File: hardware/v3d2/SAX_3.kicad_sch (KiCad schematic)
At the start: 92 parts, among them J1 joystick, J2 LED strip, J3 SSD1306 SPI, J4 MIDI OUT Y:M5 - R:M4, J5 Batt, J6 Neck - Y:O BK:B R:3.3, Q1 2N7000, U1 74HC165, U2 74HC165, U3 74HC165, U4 Teensy3.2_breadboard_friendly

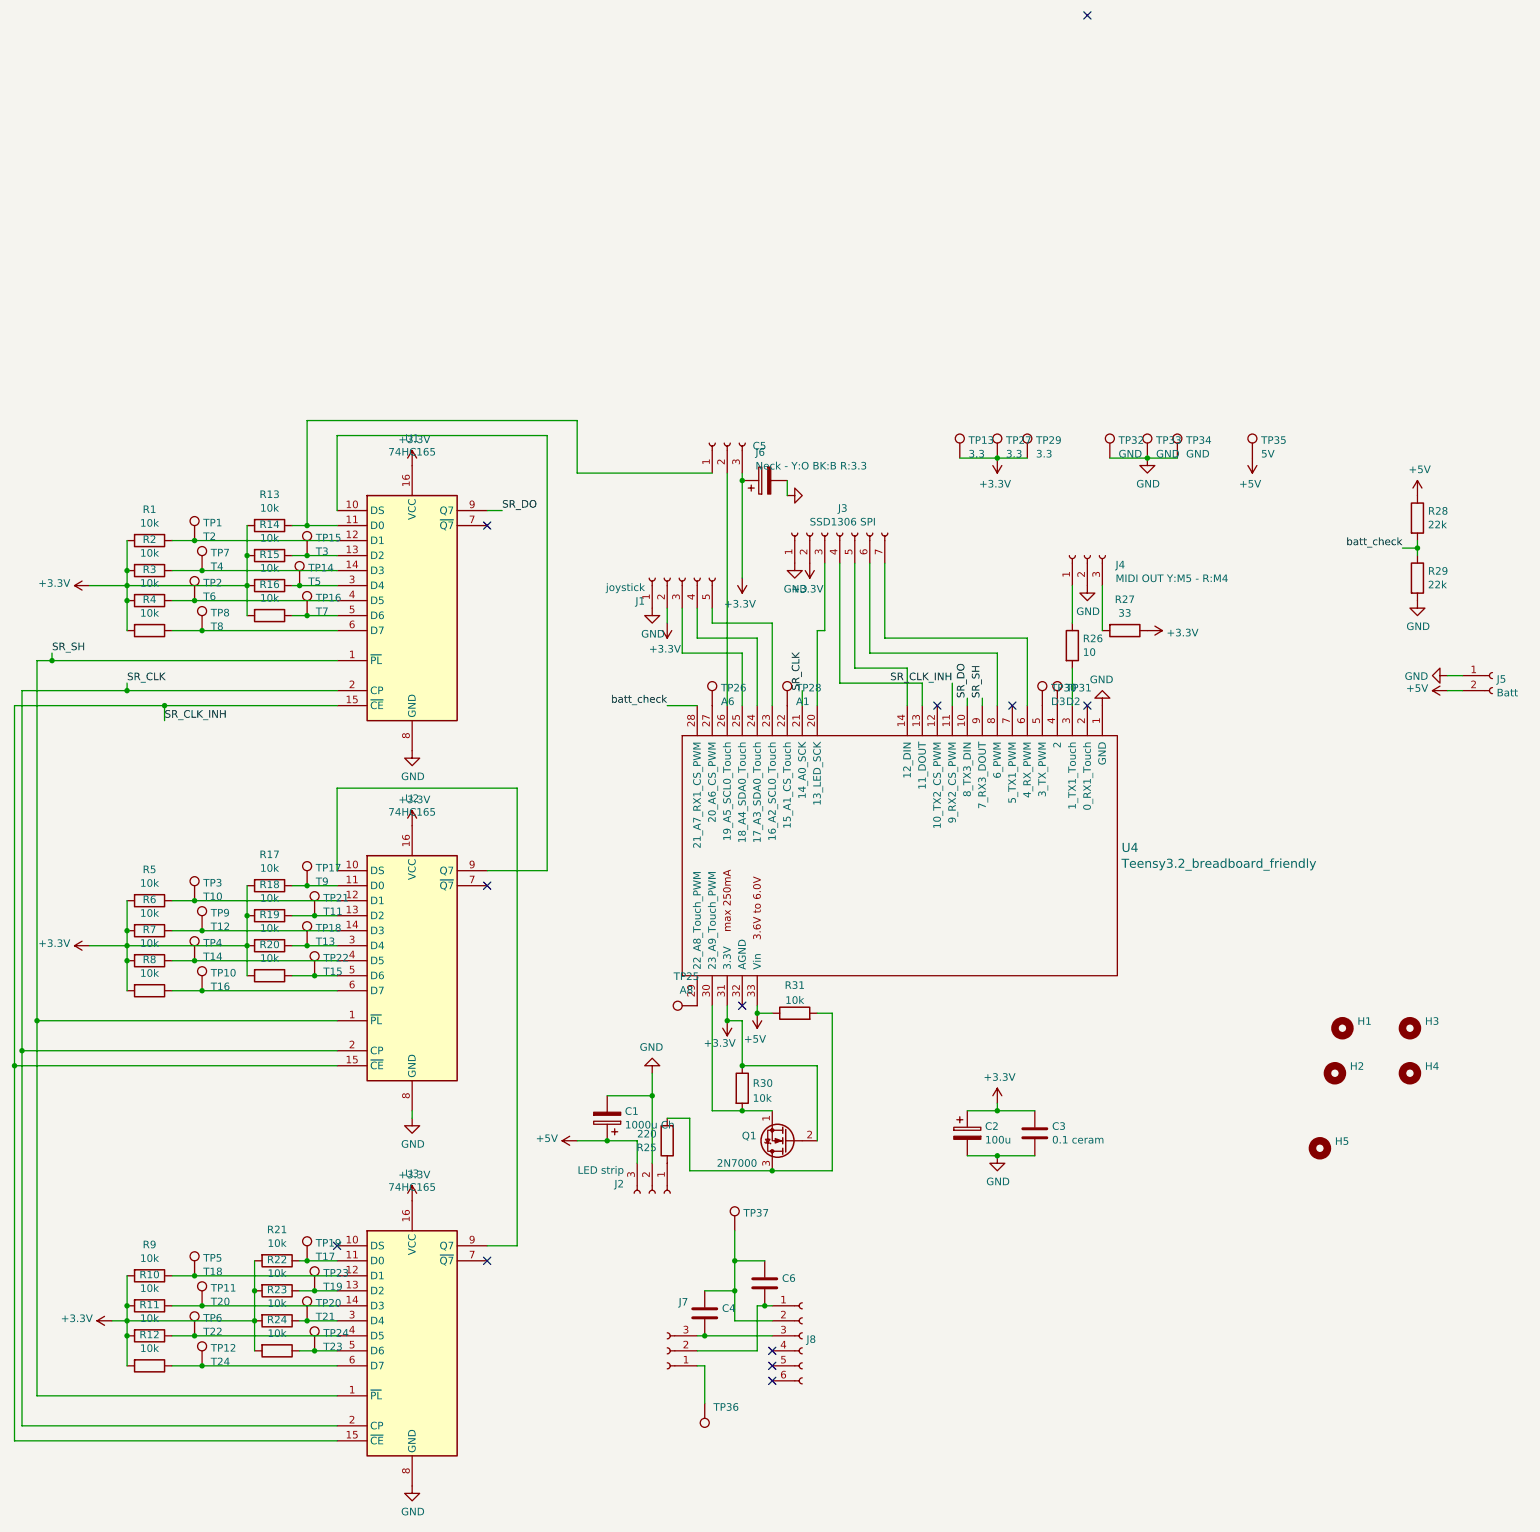
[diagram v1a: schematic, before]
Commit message: Added ADC component for battery check
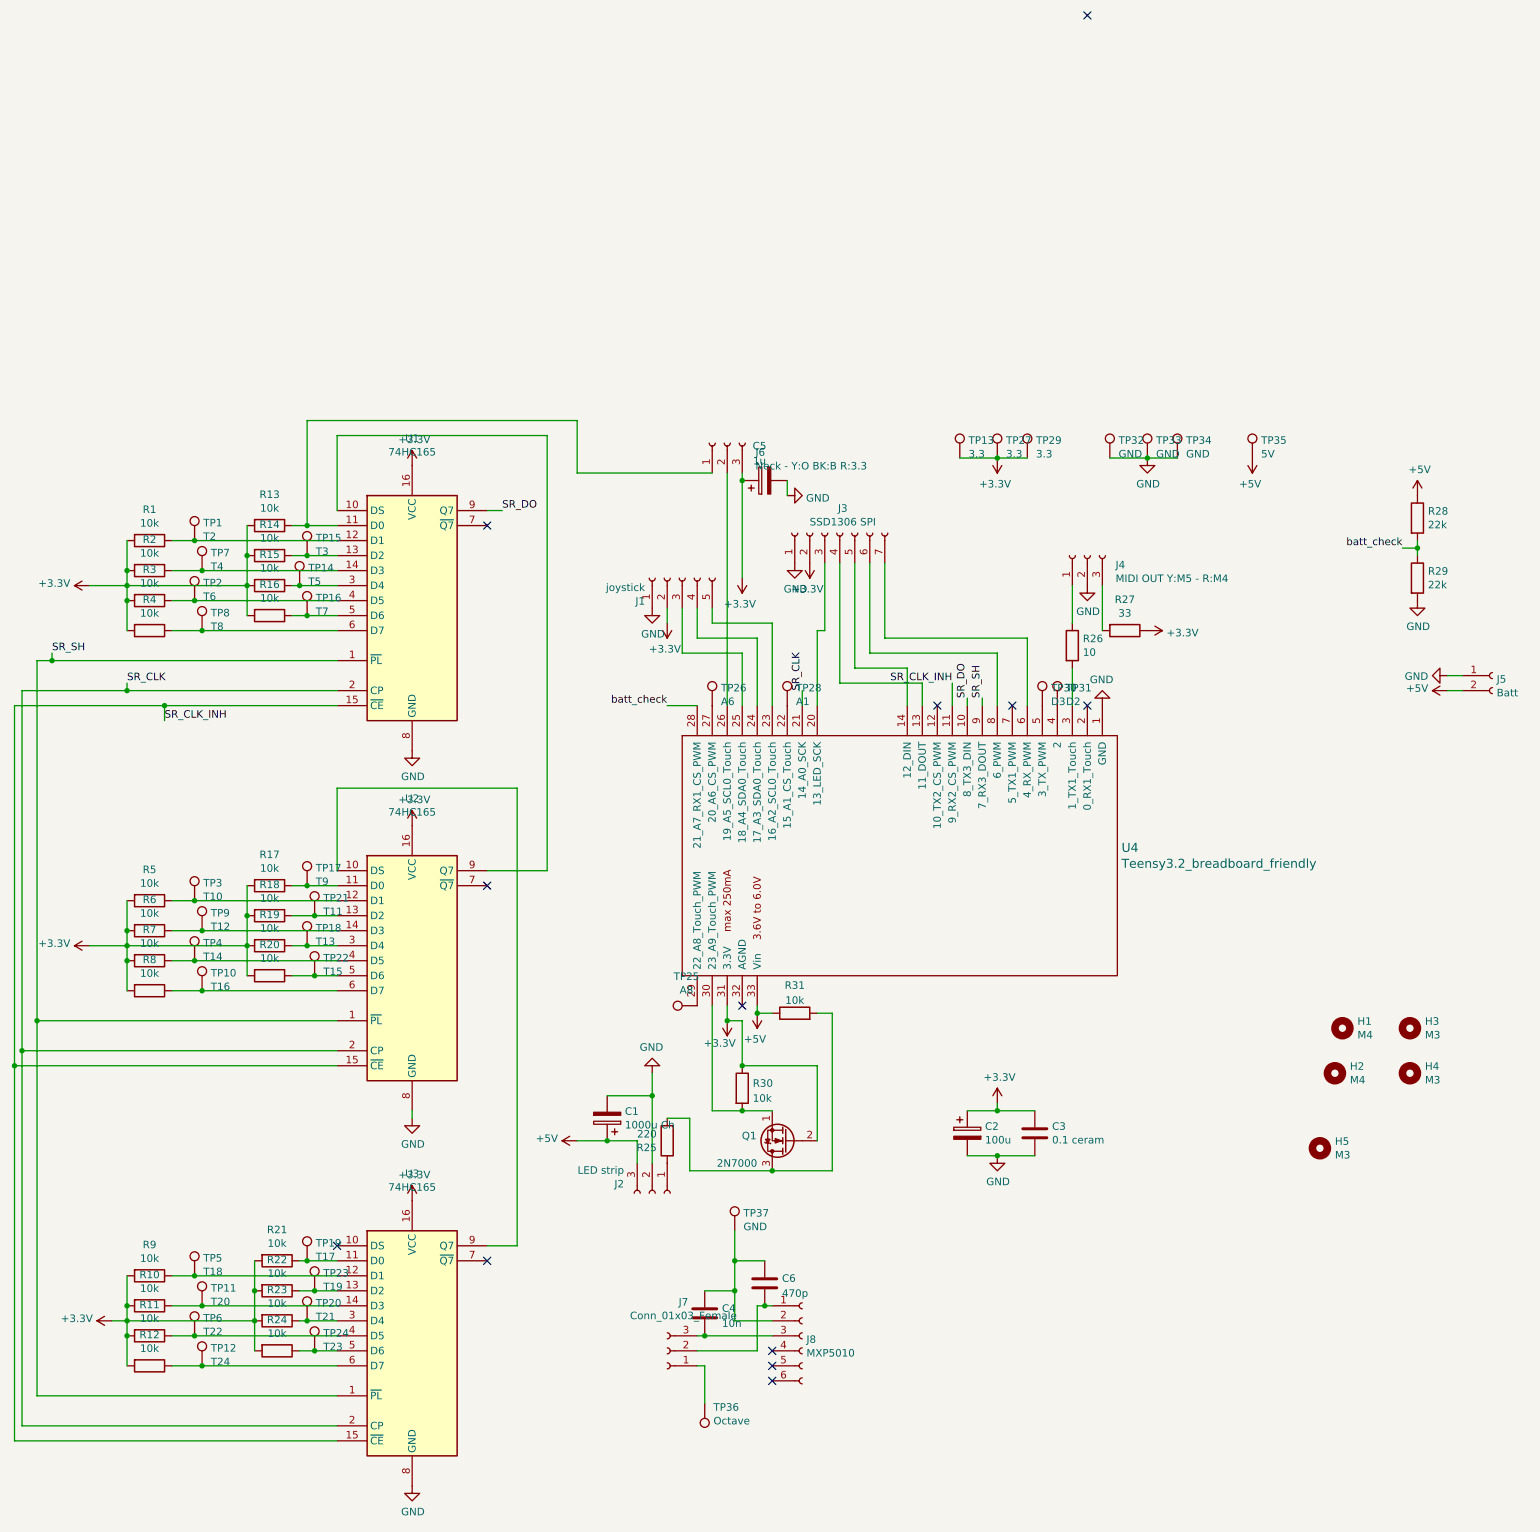
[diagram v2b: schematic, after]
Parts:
- C3: footprint (none) -> Capacitor_THT:C_Disc_D3.4mm_W2.1mm_P2.50mm
- C4: value (none) -> 10n; footprint (none) -> Capacitor_THT:C_Disc_D3.4mm_W2.1mm_P2.50mm
- C5: value (none) -> 1u; footprint (none) -> Capacitor_THT:CP_Radial_D4.0mm_P2.00mm
- C6: value (none) -> 470p; footprint (none) -> Capacitor_THT:C_Disc_D3.4mm_W2.1mm_P2.50mm
- H1, H2: value (none) -> M4; footprint (none) -> MountingHole:MountingHole_4.3mm_M4
- H3, H4, H5: value (none) -> M3; footprint (none) -> MountingHole:MountingHole_3.2mm_M3
- J7: value (none) -> Conn_01x03_Female; footprint (none) -> Connector_JST:JST_PH_B3B-PH-K_1x03_P2.00mm_Vertical
- J8: value (none) -> MXP5010; footprint (none) -> Connector_PinSocket_2.54mm:PinSocket_1x06_P2.54mm_Vertical
- TP36: value (none) -> Octave; footprint (none) -> TestPoint:TestPoint_THTPad_2.5x2.5mm_Drill1.2mm
- TP37: value (none) -> GND; footprint (none) -> TestPoint:TestPoint_THTPad_2.5x2.5mm_Drill1.2mm
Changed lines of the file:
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@@
       (effects (font (size 1.27 1.27)) (justify left))
     )
-    (property "Value" "" (id 1) (at 245.11 119.253 0)
-      (effects (font (size 1.27 1.27)) (justify left))
-    )
-    (property "Footprint" "" (id 2) (at 242.57 118.11 0)
+    (property "Value" "M4" (id 1) (at 245.11 119.253 0)
+      (effects (font (size 1.27 1.27)) (justify left))
+    )
+    (property "Footprint" "MountingHole:MountingHole_4.3mm_M4" (id 2) (at 242.57 118.11 0)
       (effects (font (size 1.27 1.27)) hide)
     )
@@
       (effects (font (size 1.27 1.27)) (justify left))
     )
-    (property "Value" "" (id 1) (at 256.54 119.253 0)
-      (effects (font (size 1.27 1.27)) (justify left))
-    )
-    (property "Footprint" "" (id 2) (at 254 118.11 0)
+    (property "Value" "M3" (id 1) (at 256.54 119.253 0)
+      (effects (font (size 1.27 1.27)) (justify left))
+    )
+    (property "Footprint" "MountingHole:MountingHole_3.2mm_M3" (id 2) (at 254 118.11 0)
       (effects (font (size 1.27 1.27)) hide)
     )
@@
       (effects (font (size 1.27 1.27)) (justify left))
     )
-    (property "Value" "" (id 1) (at 243.84 126.873 0)
-      (effects (font (size 1.27 1.27)) (justify left))
-    )
-    (property "Footprint" "" (id 2) (at 241.3 125.73 0)
+    (property "Value" "M4" (id 1) (at 243.84 126.873 0)
+      (effects (font (size 1.27 1.27)) (justify left))
+    )
+    (property "Footprint" "MountingHole:MountingHole_4.3mm_M4" (id 2) (at 241.3 125.73 0)
       (effects (font (size 1.27 1.27)) hide)
     )
@@
       (effects (font (size 1.27 1.27)) (justify left))
     )
-    (property "Value" "" (id 1) (at 256.54 126.873 0)
-      (effects (font (size 1.27 1.27)) (justify left))
-    )
-    (property "Footprint" "" (id 2) (at 254 125.73 0)
+    (property "Value" "M3" (id 1) (at 256.54 126.873 0)
+      (effects (font (size 1.27 1.27)) (justify left))
+    )
+    (property "Footprint" "MountingHole:MountingHole_3.2mm_M3" (id 2) (at 254 125.73 0)
       (effects (font (size 1.27 1.27)) hide)
     )
@@
       (effects (font (size 1.27 1.27)) (justify left))
     )
-    (property "Value" "" (id 1) (at 241.3 139.573 0)
-      (effects (font (size 1.27 1.27)) (justify left))
-    )
-    (property "Footprint" "" (id 2) (at 238.76 138.43 0)
+    (property "Value" "M3" (id 1) (at 241.3 139.573 0)
+      (effects (font (size 1.27 1.27)) (justify left))
+    )
+    (property "Footprint" "MountingHole:MountingHole_3.2mm_M3" (id 2) (at 238.76 138.43 0)
       (effects (font (size 1.27 1.27)) hide)
     )
@@
       (effects (font (size 1.27 1.27)) (justify left))
     )
-    (property "Footprint" "" (id 2) (at 191.4652 139.7 0)
+    (property "Footprint" "Capacitor_THT:C_Disc_D3.4mm_W2.1mm_P2.50mm" (id 2) (at 191.4652 139.7 0)
       (effects (font (size 1.27 1.27)) hide)
     )
@@
       (effects (font (size 1.27 1.27)) (justify left))
     )
-    (property "Value" "" (id 1) (at 151.8412 173.101 0)
-      (effects (font (size 1.27 1.27)) (justify left))
-    )
-    (property "Footprint" "" (id 2) (at 151.13 170.18 0)
+    (property "Value" "MXP5010" (id 1) (at 151.8412 173.101 0)
+      (effects (font (size 1.27 1.27)) (justify left))
+    )
+    (property "Footprint" "Connector_PinSocket_2.54mm:PinSocket_1x06_P2.54mm_Vertical" (id 2) (at 151.13 170.18 0)
       (effects (font (size 1.27 1.27)) hide)
     )
@@
     (in_bom yes) (on_board yes)
     (property "Reference" "J7" (id 0) (at 131.0132 164.465 0))
-    (property "Value" "" (id 1) (at 131.0132 166.7764 0))
-    (property "Footprint" "" (id 2) (at 128.27 172.72 0)
+    (property "Value" "Conn_01x03_Female" (id 1) (at 131.0132 166.7764 0))
+    (property "Footprint" "Connector_JST:JST_PH_B3B-PH-K_1x03_P2.00mm_Vertical" (id 2) (at 128.27 172.72 0)
       (effects (font (size 1.27 1.27)) hide)
     )
@@
       (effects (font (size 1.27 1.27)) (justify right))
     )
-    (property "Value" "" (id 1) (at 136.0932 184.5818 0)
+    (property "Value" "Octave" (id 1) (at 136.0932 184.5818 0)
       (effects (font (size 1.27 1.27)) (justify right))
     )
-    (property "Footprint" "" (id 2) (at 129.54 181.61 0)
+    (property "Footprint" "TestPoint:TestPoint_THTPad_2.5x2.5mm_Drill1.2mm" (id 2) (at 129.54 181.61 0)
       (effects (font (size 1.27 1.27)) hide)
     )
@@
       (effects (font (size 1.27 1.27)) (justify left))
     )
-    (property "Value" "" (id 1) (at 141.1732 151.7142 0)
-      (effects (font (size 1.27 1.27)) (justify left))
-    )
-    (property "Footprint" "" (id 2) (at 144.78 152.4 0)
+    (property "Value" "GND" (id 1) (at 141.1732 151.7142 0)
+      (effects (font (size 1.27 1.27)) (justify left))
+    )
+    (property "Footprint" "TestPoint:TestPoint_THTPad_2.5x2.5mm_Drill1.2mm" (id 2) (at 144.78 152.4 0)
       (effects (font (size 1.27 1.27)) hide)
     )
@@
       (effects (font (size 1.27 1.27)) (justify left))
     )
-    (property "Value" "" (id 1) (at 147.701 162.9922 0)
-      (effects (font (size 1.27 1.27)) (justify left))
-    )
-    (property "Footprint" "" (id 2) (at 145.7452 165.1 0)
+    (property "Value" "470p" (id 1) (at 147.701 162.9922 0)
+      (effects (font (size 1.27 1.27)) (justify left))
+    )
+    (property "Footprint" "Capacitor_THT:C_Disc_D3.4mm_W2.1mm_P2.50mm" (id 2) (at 145.7452 165.1 0)
       (effects (font (size 1.27 1.27)) hide)
     )
@@
     (in_bom yes) (on_board yes) (fields_autoplaced)
     (property "Reference" "C5" (id 0) (at 143.891 19.5412 90))
-    (property "Value" "" (id 1) (at 143.891 22.0781 90))
-    (property "Footprint" "" (id 2) (at 148.59 24.4348 0)
+    (property "Value" "1u" (id 1) (at 143.891 22.0781 90))
+    (property "Footprint" "Capacitor_THT:CP_Radial_D4.0mm_P2.00mm" (id 2) (at 148.59 24.4348 0)
       (effects (font (size 1.27 1.27)) hide)
     )
@@
       (effects (font (size 1.27 1.27)) hide)
     )
-    (property "Value" "" (id 1) (at 151.765 28.3738 90)
+    (property "Value" "GND" (id 1) (at 151.765 28.3738 90)
       (effects (font (size 1.27 1.27)) (justify right))
     )
@@
       (effects (font (size 1.27 1.27)) (justify left))
     )
-    (property "Value" "" (id 1) (at 137.541 168.0722 0)
-      (effects (font (size 1.27 1.27)) (justify left))
-    )
-    (property "Footprint" "" (id 2) (at 135.5852 170.18 0)
-      (effects (font (size 1.27 1.27)) hide)
-    )
+    (property "Value" "10n" (id 1) (at 137.541 168.0722 0)
+      (effects (font (size 1.27 1.27)) (justify left))
+    )
+    (property "Footprint" "Capacitor_THT:C_Disc_D3.4mm_W2.1mm_P2.50mm" (id 2) (at 135.5852 170.18 0)
+      (effects (font (size 1.27 1.27)) hide)
+    )
